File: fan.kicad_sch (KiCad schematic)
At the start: 15 parts, among them J6 Conn_01x04, J7 Conn_01x04, U10 EMC2101

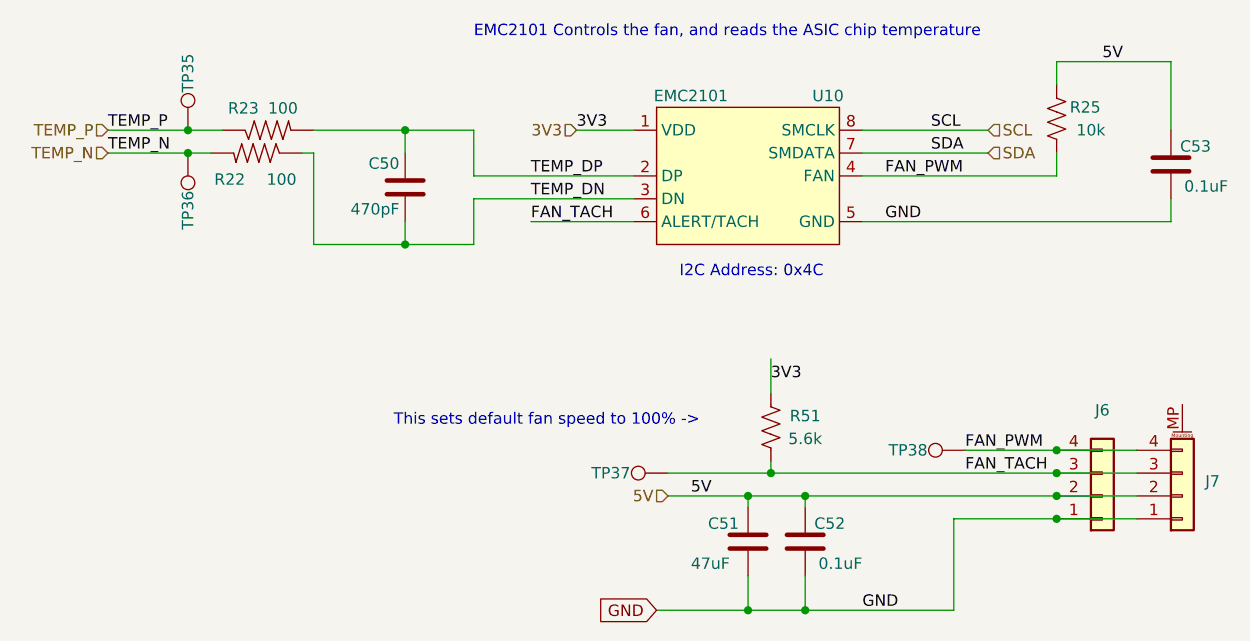
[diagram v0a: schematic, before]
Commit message: update to KiCad v9
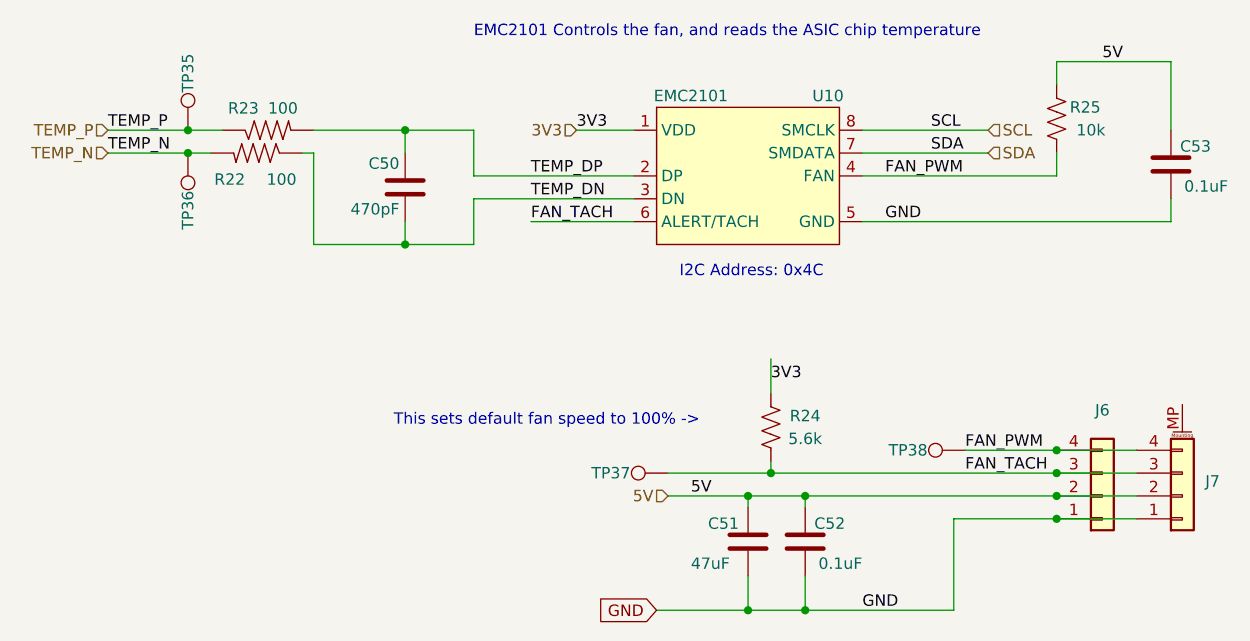
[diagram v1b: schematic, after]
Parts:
- renumbered R51 to R24
